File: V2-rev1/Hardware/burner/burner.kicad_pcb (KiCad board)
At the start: 2 copper layers, 2 parts, among them J1 ISP connector, U1 ATtiny2313-20PU

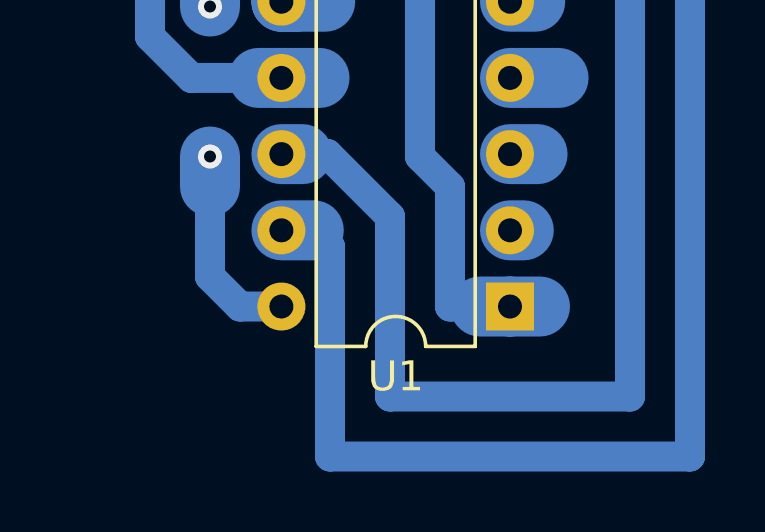
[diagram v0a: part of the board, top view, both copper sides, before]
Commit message: reinforce some copper
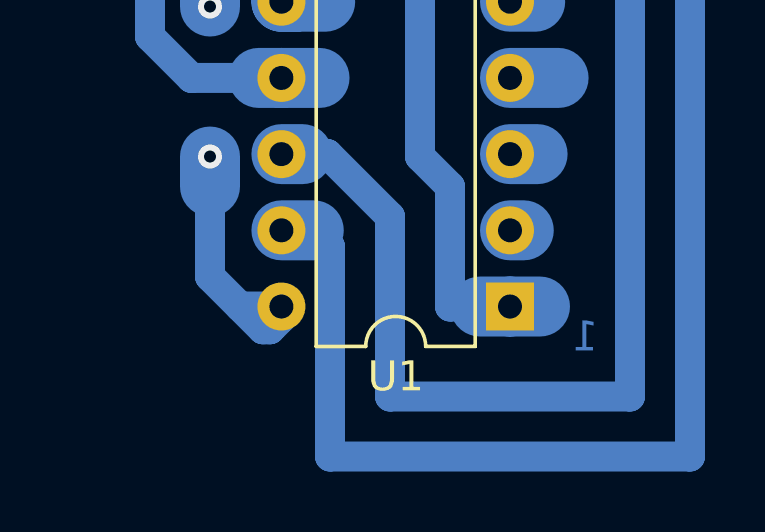
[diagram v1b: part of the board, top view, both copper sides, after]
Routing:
- net /+5V: track 25.9 -> 28.1 mm
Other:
- board text added: "1"
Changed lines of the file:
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@@
   (general
     (thickness 1.6)
-    (drawings 12)
-    (tracks 82)
+    (drawings 13)
+    (tracks 85)
     (zones 0)
     (modules 2)
@@
     )
   )
+  (gr_text 1 (at 143.5 116) (layer B.Cu)
+    (effects (font (size 1 1) (thickness 0.2)) (justify mirror))
+  )
   (target plus (at 130 117) (size 5) (width 0.05) (layer Edge.Cuts))
   (target plus (at 130 117) (size 5) (width 0.05) (layer Edge.Cuts))
@@
   (segment (start 127 89) (end 127 89) (width 1) (layer B.Cu) (net 4))
   (via (at 127 89) (size 0.8) (drill 0.4) (layers F.Cu B.Cu) (net 4))
-  (segment (start 133.38 115) (end 132 115) (width 1) (layer B.Cu) (net 6))
-  (segment (start 132 115) (end 131 114) (width 1) (layer B.Cu) (net 6))
   (segment (start 132.46 86.54) (end 131.5 87.5) (width 2) (layer B.Cu) (net 6))
   (segment (start 131.5 87.5) (end 131 88) (width 1) (layer B.Cu) (net 6))
@@
   (segment (start 131 110) (end 131 111) (width 2) (layer B.Cu) (net 6))
   (segment (start 131 114) (end 131 111) (width 1) (layer B.Cu) (net 6))
+  (segment (start 132.76 115.76) (end 131 114) (width 1) (layer B.Cu) (net 6))
+  (segment (start 133 115.76) (end 132.76 115.76) (width 1) (layer B.Cu) (net 6))
+  (segment (start 133.38 115.38) (end 133 115.76) (width 1) (layer B.Cu) (net 6))
+  (segment (start 133.38 115) (end 133.38 115.38) (width 1) (layer B.Cu) (net 6))
+  (segment (start 133.38 115) (end 132 115) (width 1) (layer B.Cu) (net 6))
   (segment (start 130 84) (end 129 85) (width 1) (layer B.Cu) (net 7))
   (segment (start 129 85) (end 129 106) (width 1) (layer B.Cu) (net 7))
